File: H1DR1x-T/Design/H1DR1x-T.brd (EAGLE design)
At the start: 34.6 x 30 mm, 30 parts, among them P1 HEXABIT_17.32_NO_P6, P2 RS-485, U1 STM32G0B1CEU6QFN_B1CEU6_STM-L, U2 MAX14840EASAT, X1 XTALL_CSTCE8M00G52

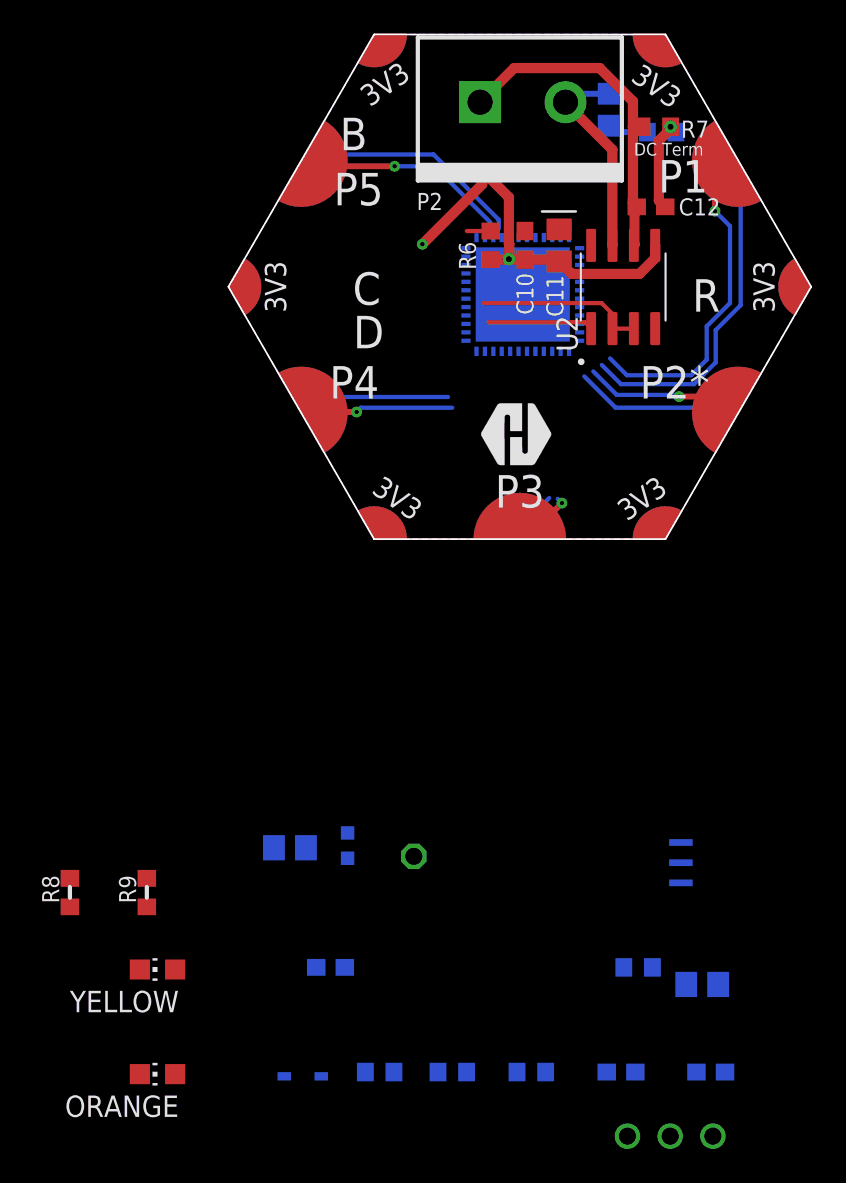
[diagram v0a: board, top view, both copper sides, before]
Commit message: - Drew PCB.
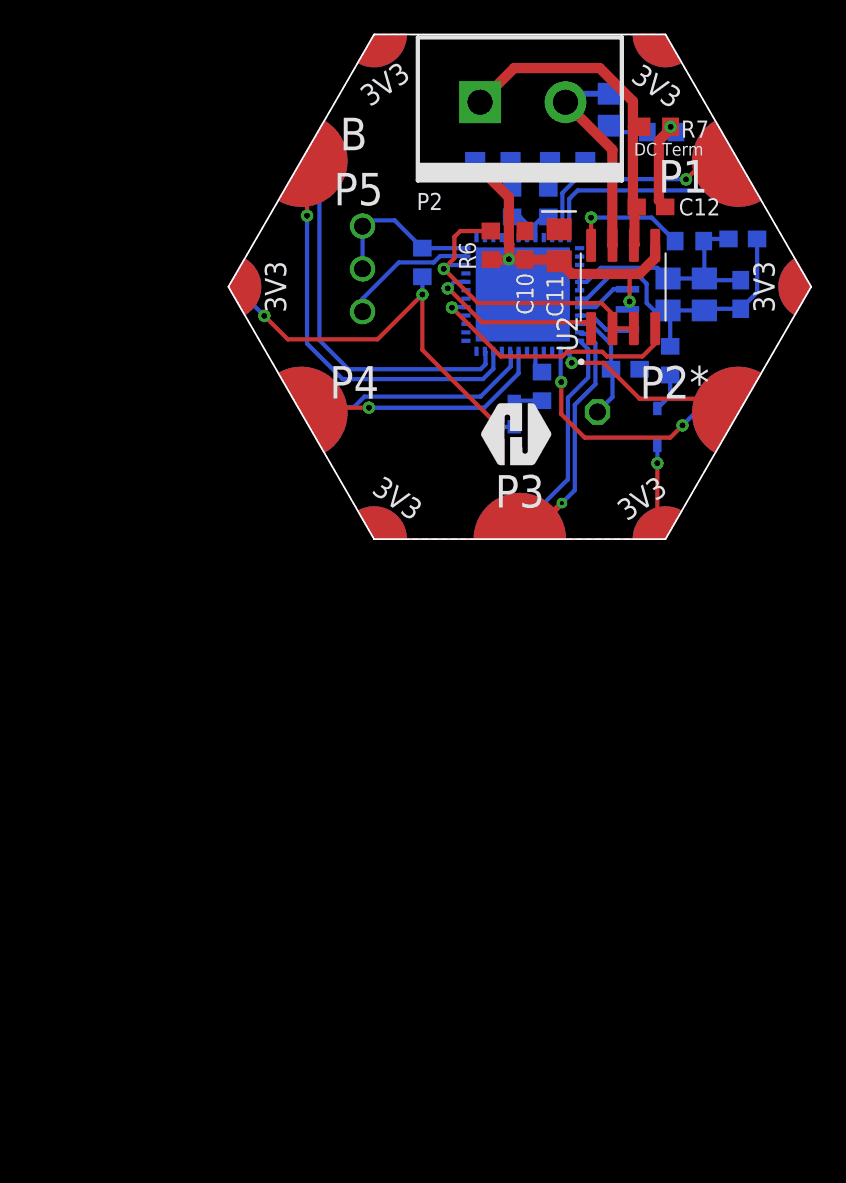
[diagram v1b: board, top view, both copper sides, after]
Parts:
- removed ORANGE, YELLOW: (no value), HEXABITZ_USER_INTERFACE_PARTS:CHIP-LED0805
- added ORG, YLW: (no value), HEXABITZ_USER_INTERFACE_PARTS:CHIP-LED0805
- moved SWD 54.7 mm to (-9.27, 16.1), turned to 270 degrees
- moved C6 50.1 mm to (13.3, 17.9), turned to 180 degrees
- moved R8 49.9 mm to (1.78, 20.1), flipped to the bottom, turned to 270 degrees
- moved R3 48.2 mm to (-5.71, 16.5), turned to 90 degrees
- moved R9 46.4 mm to (-0.38, 20.1), flipped to the bottom, turned to 270 degrees
- moved C5 46.3 mm to (13.2, 14.6), turned to 270 degrees
- moved R1 44.2 mm to (9.02, 10.7), turned to 90 degrees
- moved D5 44.0 mm to (8.26, 6.73), turned to 270 degrees
- moved FB1 43.3 mm to (10.2, 17.8)
- moved C1 41.0 mm to (11.0, 14.6), turned to 270 degrees
- moved R2 40.8 mm to (1.40, 9.14), turned to 270 degrees
- moved C4 39.8 mm to (8.89, 14.6), turned to 270 degrees
- moved C3 39.6 mm to (6.35, 10.2), turned to 180 degrees
- moved X1 33.0 mm to (6.48, 13.7), turned to 180 degrees
- moved R 28.6 mm to (4.70, 7.62)
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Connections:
- net GND: now also ORG.C, YLW.C; no longer ORANGE.C, YELLOW.C
- net N$12: now also ORG.A; no longer ORANGE.A
- net N$13: now also YLW.A; no longer YELLOW.A
- net USART3_RX: now also P1.PAD_PD5; no longer P1.PAD_PD4
- net USART3_TX: now also P1.PAD_PU5; no longer P1.PAD_PU4
- net USART4_RX: now also P1.PAD_PD3; no longer P1.PAD_PD1
- net USART4_TX: now also P1.PAD_PU3; no longer P1.PAD_PU1
- net USART5_RX: now also P1.PAD_PD4; no longer P1.PAD_PD5
- net USART5_TX: now also P1.PAD_PU4; no longer P1.PAD_PU5
- net USART6_RX: now also P1.PAD_PD1; no longer P1.PAD_PD3
- net USART6_TX: now also P1.PAD_PU1; no longer P1.PAD_PU3
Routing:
- net GND: track 23.1 -> 46.8 mm, vias 3 -> 6
- net VSSA: track 0.00 -> 18.5 mm
- net UART1_TX: track 0.00 -> 15.6 mm, vias 0 -> 1
- net USART3_TX: track 8.89 -> 23.9 mm
- net VDDA: track 0.00 -> 15.0 mm
- net USART3_RX: track 8.65 -> 23.2 mm
- net VDD: track 0.00 -> 12.1 mm, vias 0 -> 2
- net USART6_RX: track 2.47 -> 12.6 mm
- net USART6_TX: track 3.67 -> 13.4 mm
- net CLK: track 0.00 -> 9.51 mm
- net DATA: track 0.00 -> 7.97 mm
- net UART1_RTS: track 11.5 -> 19.2 mm, vias 0 -> 1
- net USART4_RX: track 20.4 -> 13.0 mm
- net N$4: track 0.00 -> 6.80 mm
- net USART2_RX: track 9.34 -> 15.0 mm, vias 0 -> 2
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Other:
- board text removed: "C"
- board text removed: "D"
- board text removed: "R"

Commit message: - Regenerated Documentation. - BOM is ready. - Regenerated output files.
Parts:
- D2: value (none) -> Yellow
- D3: value (none) -> Orange
- renumbered ORG to D3, YLW to D2
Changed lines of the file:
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@@
 <attribute name="VALUE" x="1.524" y="20.701" size="1.016" layer="28" rot="MR270"/>
 </element>
-<element name="YLW" library="HEXABITZ_USER_INTERFACE_PARTS" library_urn="urn:adsk.eagle:library:20064563" package="CHIP-LED0805" package3d_urn="urn:adsk.eagle:package:15818/2" value="" x="2.921" y="22.479" smashed="yes" rot="MR90">
+<element name="D2" library="HEXABITZ_USER_INTERFACE_PARTS" library_urn="urn:adsk.eagle:library:20064563" package="CHIP-LED0805" package3d_urn="urn:adsk.eagle:package:15818/2" value="Yellow" x="2.921" y="22.479" smashed="yes" rot="MR90">
 <attribute name="DESCRIPTION" value="" x="2.921" y="22.479" size="1.778" layer="28" rot="MR90" display="off"/>
 <attribute name="MFN" value="" x="2.921" y="22.479" size="1.778" layer="28" rot="MR90" display="off"/>
@@
 <attribute name="VALUE" x="1.651" y="25.019" size="1.27" layer="28" rot="MR180"/>
 </element>
-<element name="ORG" library="HEXABITZ_USER_INTERFACE_PARTS" library_urn="urn:adsk.eagle:library:20064563" package="CHIP-LED0805" package3d_urn="urn:adsk.eagle:package:15818/2" value="" x="-1.524" y="22.479" smashed="yes" rot="MR270">
+<element name="D3" library="HEXABITZ_USER_INTERFACE_PARTS" library_urn="urn:adsk.eagle:library:20064563" package="CHIP-LED0805" package3d_urn="urn:adsk.eagle:package:15818/2" value="Orange" x="-1.524" y="22.479" smashed="yes" rot="MR270">
 <attribute name="DESCRIPTION" value="" x="-1.524" y="22.479" size="1.778" layer="28" rot="MR270" display="off"/>
 <attribute name="MFN" value="" x="-1.524" y="22.479" size="1.778" layer="28" rot="MR270" display="off"/>
@@
 <contactref element="U1" pad="49"/>
 <contactref element="D1" pad="C"/>
-<contactref element="ORG" pad="C"/>
-<contactref element="YLW" pad="C"/>
+<contactref element="D3" pad="C"/>
+<contactref element="D2" pad="C"/>
 <wire x1="8.255" y1="7.831" x2="9.017" y2="8.593" width="0.254" layer="16"/>
 <wire x1="9.017" y1="8.593" x2="9.017" y2="9.818" width="0.254" layer="16"/>
@@
 <signal name="N$12">
 <contactref element="R9" pad="1"/>
-<contactref element="ORG" pad="A"/>
+<contactref element="D3" pad="A"/>
 <wire x1="-0.381" y1="20.916" x2="-0.474" y2="21.009" width="0.254" layer="16"/>
 <wire x1="-0.474" y1="21.009" x2="-0.474" y2="22.479" width="0.254" layer="16"/>
@@
 <signal name="N$13">
 <contactref element="R8" pad="1"/>
-<contactref element="YLW" pad="A"/>
+<contactref element="D2" pad="A"/>
 <wire x1="1.778" y1="20.916" x2="1.778" y2="22.386" width="0.254" layer="16"/>
 <wire x1="1.778" y1="22.386" x2="1.871" y2="22.479" width="0.254" layer="16"/>
